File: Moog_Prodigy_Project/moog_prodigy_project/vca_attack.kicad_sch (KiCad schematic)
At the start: 14 parts, among them U21 MC14007UBCP, U22 MC14007UBCP, U23 MC14007UBCP

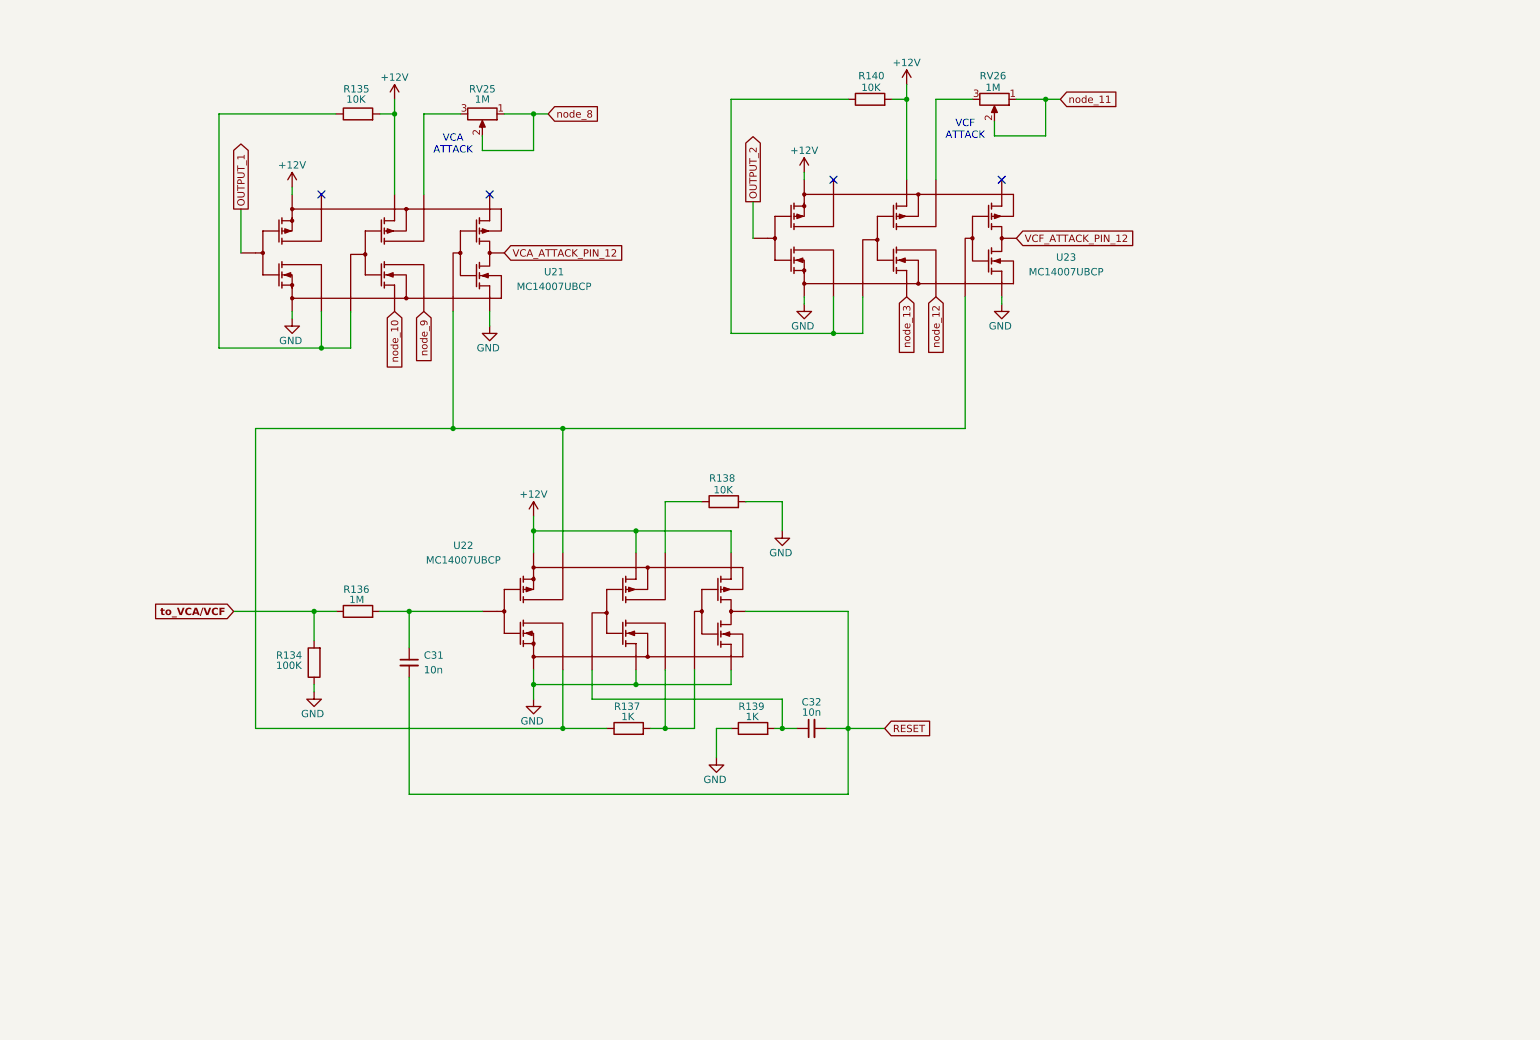
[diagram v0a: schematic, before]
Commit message: Dodao u napomenu za linearne i logaritamske potenciometre, NE555 i sa 4007 semom spojena u jedno, dodati kvalitetni kondenzatori, ostao simbol za 4007 da izenim kao sto je jocke
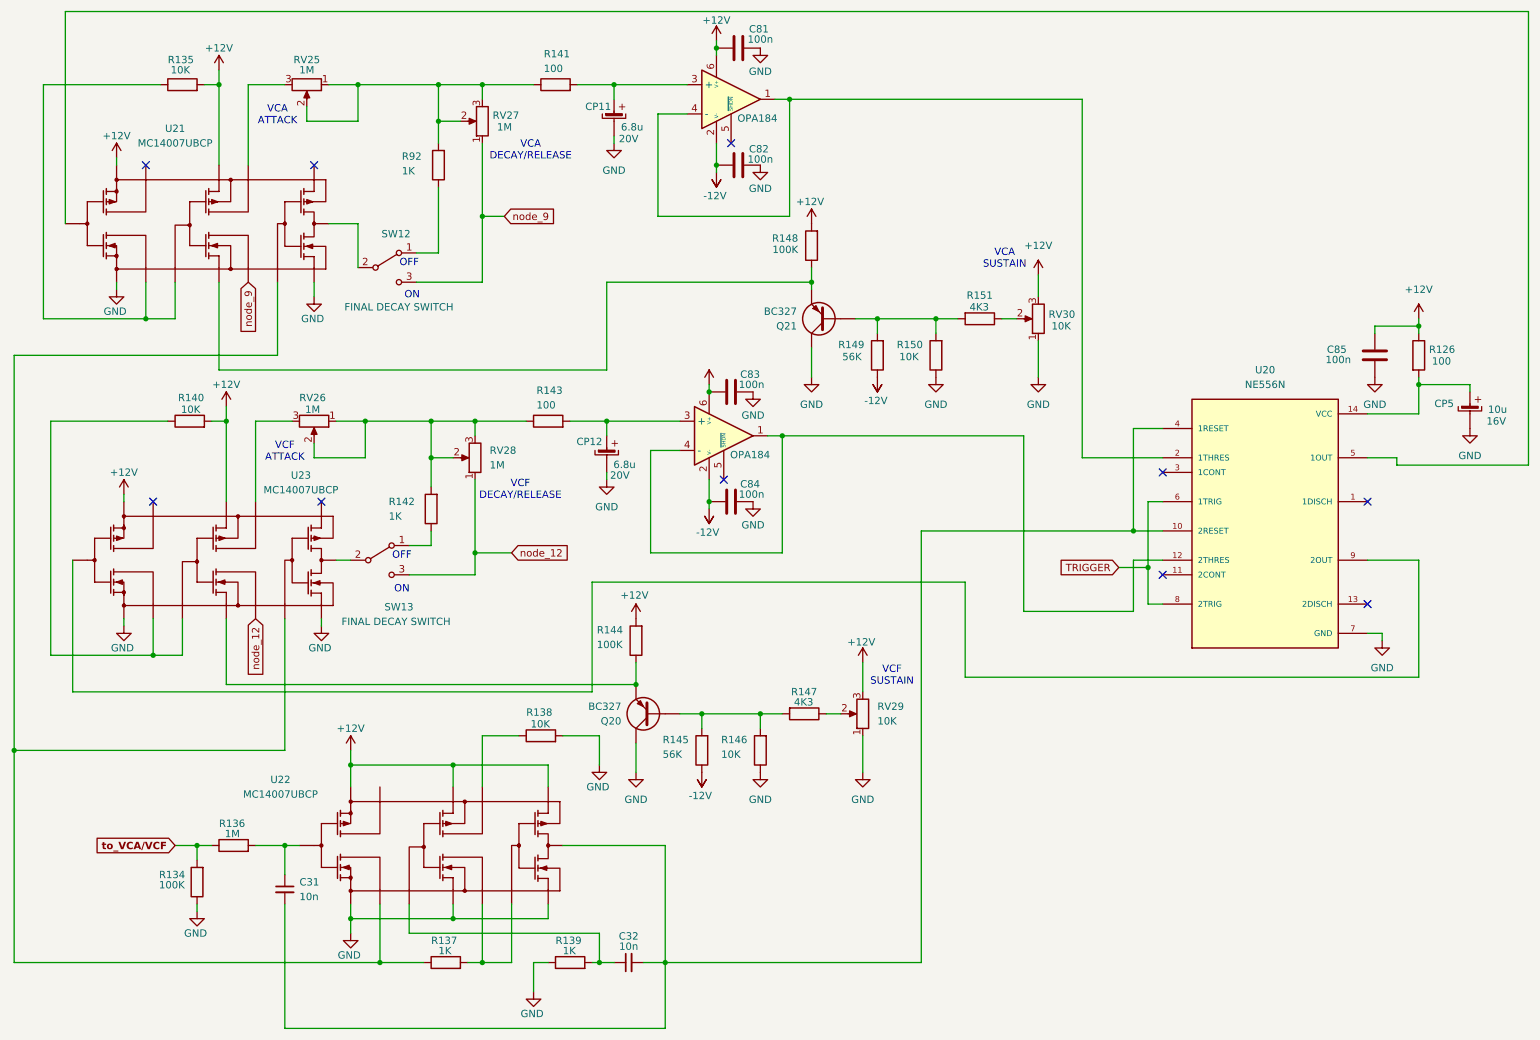
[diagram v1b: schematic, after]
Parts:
- added C81, C82, C83, C84, C85: 100n, Capacitor_THT:CP_Radial_D5.0mm_P2.50mm, symbol Device:C
- added CP11, CP12: 6.8u, Capacitor_THT:CP_Radial_D5.0mm_P2.50mm, symbol elektrolitski:elektrolit
- added CP5: 10u, Capacitor_THT:CP_Radial_D5.0mm_P2.50mm, symbol elektrolitski:elektrolit
- added Q20, Q21: BC327, Package_TO_SOT_THT:TO-92_Inline, symbol Transistor_BJT:BC556
- added R126, R141, R143: 100, Resistor_THT:R_Axial_DIN0207_L6.3mm_D2.5mm_P7.62mm_Horizontal, symbol Device:R
- added R142, R92: 1K, Resistor_THT:R_Axial_DIN0207_L6.3mm_D2.5mm_P7.62mm_Horizontal, symbol Device:R
- added R144, R148: 100K, Resistor_THT:R_Axial_DIN0207_L6.3mm_D2.5mm_P7.62mm_Horizontal, symbol Device:R
- added R145, R149: 56K, Resistor_THT:R_Axial_DIN0207_L6.3mm_D2.5mm_P7.62mm_Horizontal, symbol Device:R
- added R146, R150: 10K, Resistor_THT:R_Axial_DIN0207_L6.3mm_D2.5mm_P7.62mm_Horizontal, symbol Device:R
- added R147, R151: 4K3, Resistor_THT:R_Axial_DIN0207_L6.3mm_D2.5mm_P7.62mm_Horizontal, symbol Device:R
- added RV27, RV28: 1M, Potentiometer_THT:Potentiometer_ACP_CA9-V10_Vertical, symbol Device:R_Potentiometer
- added RV29, RV30: 10K, Potentiometer_THT:Potentiometer_ACP_CA9-V10_Vertical, symbol Device:R_Potentiometer
- added SW12, SW13: FINAL DECAY SWITCH, ATE1D-2M3-10-Z_1x2:SW_ATE1D-2M3-10-Z, symbol Switch:SW_SPDT
- added U20: NE556N, NE556N:DIP794W45P254L1930H508Q14, symbol NE556N:NE556N
- added U26, U27: OPA184, Package_DIP:DIP-8_W7.62mm, symbol Amplifier_Operational:OPA310SxDBV
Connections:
- net OUTPUT_1 is gone; now on net node_9: U21.
- net OUTPUT_2 is gone; now on net node_12: U23.
- net VCA_ATTACK_PIN_12 is gone; now on net node_9: U21.
- net VCF_ATTACK_PIN_12 is gone; now on net node_12: U23.
- net node_10 is gone; now on net node_9: U21.
- net node_13 is gone; now on net node_12: U23.
- net +12V: now also C81.2, C83.2, C85.1, R126.1, R144.2, R148.2, RV29.3, RV30.3, U26.6 (V+), U27.6 (V+)
- net GND: now also C81.1, C82.1, C83.1, C84.1, C85.2, CP11., CP12., CP5., Q20. (E), Q21. (E), R146.1, R150.1, RV29.1, RV30.1, U20.7 (GND)
- net node_12: now also RV28.1, SW13.3 (C)
- net node_9: now also RV27.1, SW12.3 (C)
- net RESET: no longer names the net of C31.2, C32.2, U22.
- net RESET: now also U20.10 (2RESET), U20.4 (1RESET)
- net node_11: no longer names the net of RV26.1, RV26.2
- net node_11: now also R142.2, R143.1, RV28.2, RV28.3
- net node_8: no longer names the net of RV25.1, RV25.2
- net node_8: now also R141.1, R92.2, RV27.2, RV27.3
- new net: Q21. (E), R149.2, R150.2, R151.2
- new net: CP5., R126.2, U20.14 (VCC)
- new net: Q20. (E), R145.2, R146.2, R147.2
- new net: Q20. (E), R144.1, U23.
- new net: Q21. (E), R148.1, U21.
- new net: CP11., R141.2, U26.3 (+)
- new net: R137.1, U21., U22., U23.
- new net: U20.2 (1THRES), U26.1, U26.4 (-)
- new net: CP12., R143.2, U27.3 (+)
- new net: R92.1, SW12.1 (A)
- new net: U20.5 (1OUT), U21.
- new net: SW12.2 (B), U21.
- new net: R151.1, RV30.2
- new net: R147.1, RV29.2
- new net: U20.12 (2THRES), U27.1, U27.4 (-)
- new net: R142.1, SW13.1 (A)
- new net: U20.9 (2OUT), U23.
- new net: SW13.2 (B), U23.
- new net -12V: C82.2, C84.2, R145.1, R149.1, U26.2 (V-), U27.2 (V-)
- new net TRIGGER: U20.6 (1TRIG), U20.8 (2TRIG)
- no-connect marks 4 -> 10
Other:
- note added: "OFF"
- note added: "ON"
- note added: "VCA DECAY/RELEASE"
- note added: "VCA SUSTAIN"
- note added: "VCF DECAY/RELEASE"
- note added: "VCF SUSTAIN"
- moved on the sheet: C31, C32, R134, R135, R136, R137, R138, R139, R140, RV25, RV26, U21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
